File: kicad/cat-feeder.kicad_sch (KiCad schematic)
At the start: 7 parts, among them M1 Motor_Servo, M2 Motor_DC, SW1 SW_SPST, SW2 SW_Push, U1 NodeMCU1.0(ESP-12E), U2 L298N

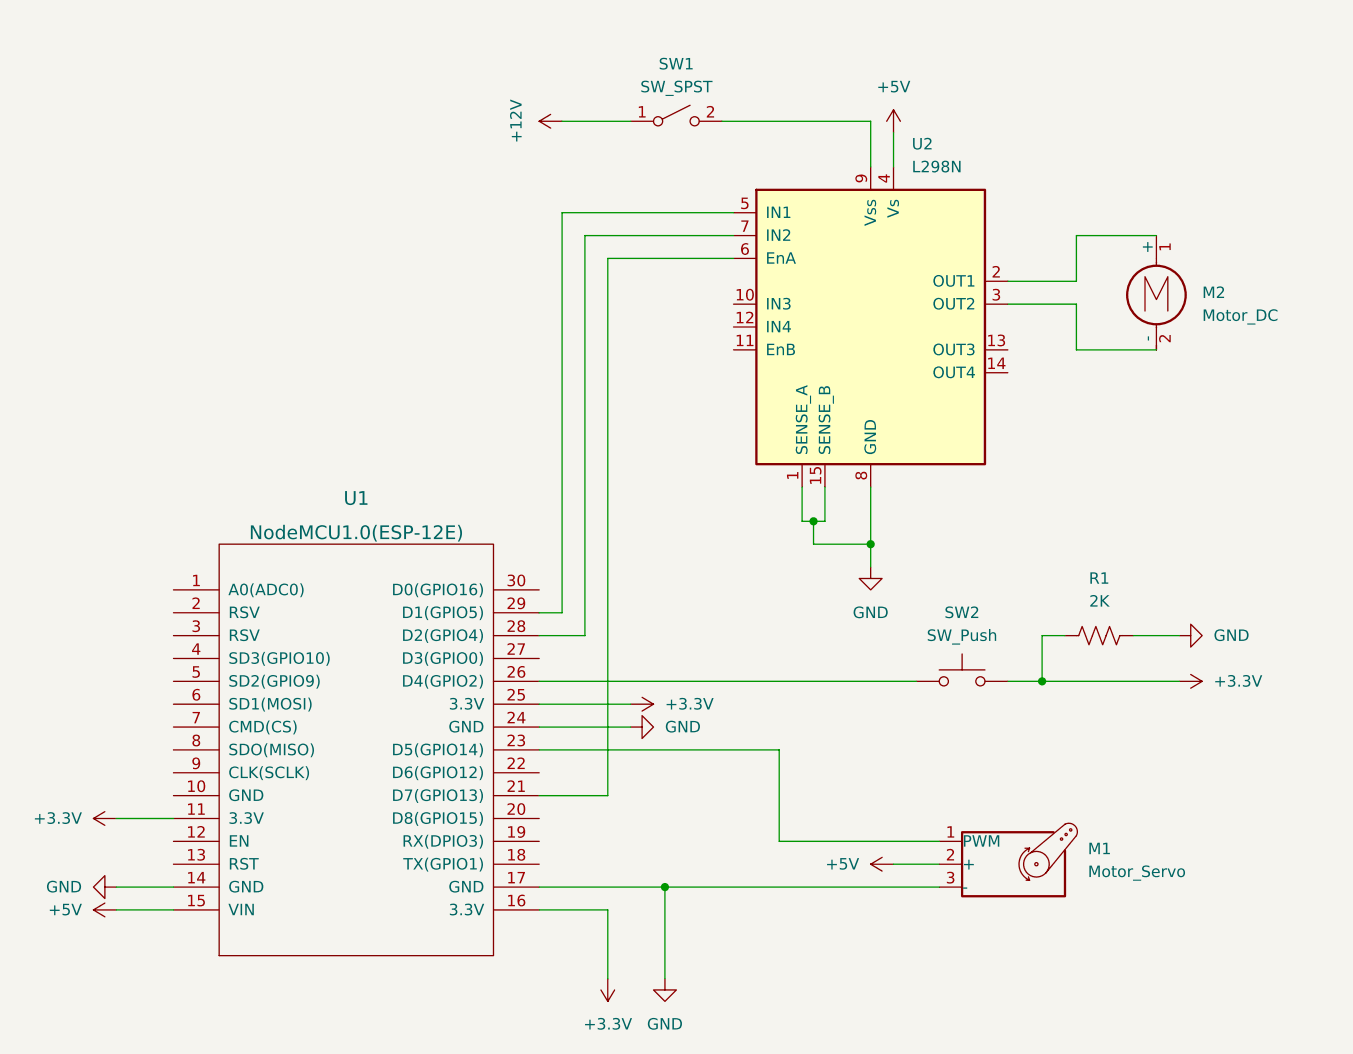
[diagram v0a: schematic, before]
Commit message: add ready and power LEDs to schematic
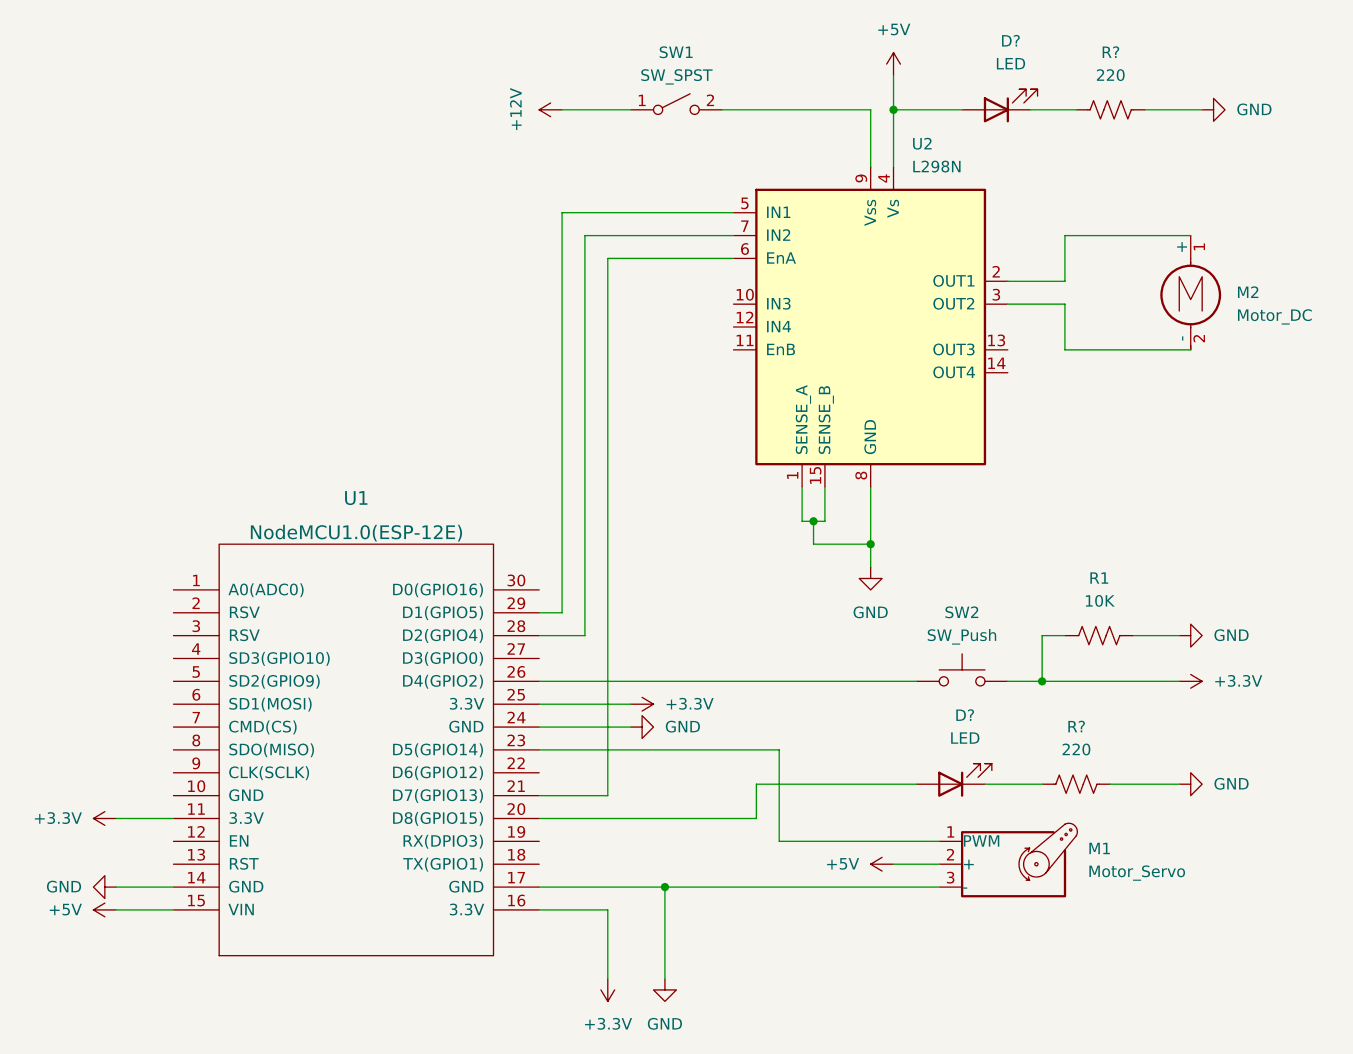
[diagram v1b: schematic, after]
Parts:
- added D? (x2): LED, symbol Device:LED
- added R? (x2): 220, symbol Device:R_US
- R1: value 2K -> 10K
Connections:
- net +5V: now also D?.2 (A)
- net GND: now also R?.2, R?.2
- net at U1.20 (D8(GPIO15)): now also D?.2 (A)
- new net: D?.1 (K), R?.1 (x2)
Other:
- moved on the sheet: M2, SW1

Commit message: change LED resistors to 470 ohm
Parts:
- R? (x2): value 220 -> 470
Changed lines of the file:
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@@
     (in_bom yes) (on_board yes) (fields_autoplaced)
     (property "Reference" "R?" (id 0) (at 166.37 107.95 90))
-    (property "Value" "220" (id 1) (at 166.37 110.49 90))
+    (property "Value" "470" (id 1) (at 166.37 110.49 90))
     (property "Footprint" "" (id 2) (at 166.624 113.284 90)
       (effects (font (size 1.27 1.27)) hide)
@@
     (in_bom yes) (on_board yes) (fields_autoplaced)
     (property "Reference" "R?" (id 0) (at 170.18 33.02 90))
-    (property "Value" "220" (id 1) (at 170.18 35.56 90))
+    (property "Value" "470" (id 1) (at 170.18 35.56 90))
     (property "Footprint" "" (id 2) (at 170.434 38.354 90)
       (effects (font (size 1.27 1.27)) hide)
@@
     )
     (path "/98ff483f-c680-47cd-8f24-3acc0f5d4892"
-      (reference "R?") (unit 1) (value "220") (footprint "")
+      (reference "R?") (unit 1) (value "470") (footprint "")
     )
     (path "/ad93abf6-cd91-4097-ad5f-237abd0904a2"
-      (reference "R?") (unit 1) (value "220") (footprint "")
+      (reference "R?") (unit 1) (value "470") (footprint "")
     )
     (path "/3f36e4ce-1226-4af1-b183-1986a281738d"

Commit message: fixes incorrect button wiring in schematic
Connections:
- net +3.3V: no longer R1.1
- net at SW2.1, U1.26 (D4(GPIO2)): now also R1.1
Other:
- moved on the sheet: R1
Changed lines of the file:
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@@
     (company "Barrett Otte")
   )
-  (junction (at 162.56 102.87) (diameter 0) (color 0 0 0 0)
+  (junction (at 139.7 87.63) (diameter 0) (color 0 0 0 0)
   )
   (junction (at 143.51 87.63) (diameter 0) (color 0 0 0 0)
   )
+  (junction (at 116.84 102.87) (diameter 0) (color 0 0 0 0)
+  )
   (junction (at 146.05 39.37) (diameter 0) (color 0 0 0 0)
   )
@@
     (stroke (width 0) (type default) (color 0 0 0 0))
   )
-  (wire (pts (xy 137.16 87.63) (xy 143.51 87.63))
+  (wire (pts (xy 137.16 87.63) (xy 139.7 87.63))
     (stroke (width 0) (type default) (color 0 0 0 0))
   )
@@
     (stroke (width 0) (type default) (color 0 0 0 0))
   )
-  (wire (pts (xy 106.68 102.87) (xy 148.59 102.87))
+  (wire (pts (xy 106.68 102.87) (xy 116.84 102.87))
     (stroke (width 0) (type default) (color 0 0 0 0))
   )
@@
     (stroke (width 0) (type default) (color 0 0 0 0))
   )
-  (wire (pts (xy 158.75 102.87) (xy 162.56 102.87))
+  (wire (pts (xy 158.75 102.87) (xy 177.8 102.87))
     (stroke (width 0) (type default) (color 0 0 0 0))
   )
@@
     (stroke (width 0) (type default) (color 0 0 0 0))
   )
+  (wire (pts (xy 139.7 97.79) (xy 139.7 87.63))
+    (stroke (width 0) (type default) (color 0 0 0 0))
+  )
   (wire (pts (xy 59.69 118.11) (xy 66.04 118.11))
     (stroke (width 0) (type default) (color 0 0 0 0))
@@
     (stroke (width 0) (type default) (color 0 0 0 0))
   )
-  (wire (pts (xy 165.1 97.79) (xy 162.56 97.79))
+  (wire (pts (xy 116.84 97.79) (xy 121.92 97.79))
     (stroke (width 0) (type default) (color 0 0 0 0))
   )
@@
     (stroke (width 0) (type default) (color 0 0 0 0))
   )
+  (wire (pts (xy 116.84 97.79) (xy 116.84 102.87))
+    (stroke (width 0) (type default) (color 0 0 0 0))
+  )
   (wire (pts (xy 114.3 115.57) (xy 106.68 115.57))
     (stroke (width 0) (type default) (color 0 0 0 0))
@@
     (stroke (width 0) (type default) (color 0 0 0 0))
   )
-  (wire (pts (xy 162.56 102.87) (xy 177.8 102.87))
-    (stroke (width 0) (type default) (color 0 0 0 0))
-  )
-  (wire (pts (xy 172.72 97.79) (xy 177.8 97.79))
+  (wire (pts (xy 129.54 97.79) (xy 139.7 97.79))
     (stroke (width 0) (type default) (color 0 0 0 0))
   )
@@
     (stroke (width 0) (type default) (color 0 0 0 0))
   )
-  (wire (pts (xy 162.56 97.79) (xy 162.56 102.87))
+  (wire (pts (xy 116.84 102.87) (xy 148.59 102.87))
+    (stroke (width 0) (type default) (color 0 0 0 0))
+  )
+  (wire (pts (xy 139.7 87.63) (xy 143.51 87.63))
     (stroke (width 0) (type default) (color 0 0 0 0))
   )
@@
     (pin "1")
   )
-  (symbol (lib_id "Device:R_US") (at 168.91 97.79 90) (unit 1)
-    (in_bom yes) (on_board yes) (fields_autoplaced)
-    (property "Reference" "R1" (id 0) (at 168.91 91.44 90))
-    (property "Value" "10K" (id 1) (at 168.91 93.98 90))
-    (property "Footprint" "" (id 2) (at 169.164 96.774 90)
-      (effects (font (size 1.27 1.27)) hide)
-    )
-    (property "Datasheet" "~" (id 3) (at 168.91 97.79 0)
-      (effects (font (size 1.27 1.27)) hide)
-    )
-    (pin "1")
-    (pin "2")
-  )
-  (symbol (lib_id "power:GND") (at 177.8 97.79 90) (unit 1)
-    (in_bom yes) (on_board yes) (fields_autoplaced)
-    (property "Reference" "#PWR012" (id 0) (at 184.15 97.79 0)
-      (effects (font (size 1.27 1.27)) hide)
-    )
-    (property "Value" "GND" (id 1) (at 181.61 97.7899 90)
-      (effects (font (size 1.27 1.27)) (justify right))
-    )
-    (property "Footprint" "" (id 2) (at 177.8 97.79 0)
-      (effects (font (size 1.27 1.27)) hide)
-    )
-    (property "Datasheet" "" (id 3) (at 177.8 97.79 0)
-      (effects (font (size 1.27 1.27)) hide)
-    )
-    (pin "1")
+  (symbol (lib_id "Device:R_US") (at 125.73 97.79 90) (unit 1)
+    (in_bom yes) (on_board yes) (fields_autoplaced)
+    (property "Reference" "R1" (id 0) (at 125.73 91.44 90))
+    (property "Value" "10K" (id 1) (at 125.73 93.98 90))
+    (property "Footprint" "" (id 2) (at 125.984 96.774 90)
+      (effects (font (size 1.27 1.27)) hide)
+    )
+    (property "Datasheet" "~" (id 3) (at 125.73 97.79 0)
+      (effects (font (size 1.27 1.27)) hide)
+    )
+    (pin "1")
+    (pin "2")
   )
   (symbol (lib_id "power:GND") (at 59.69 125.73 270) (unit 1)
@@
       (reference "#PWR011") (unit 1) (value "+5V") (footprint "")
     )
-    (path "/6f496f53-838b-4575-96a9-2ac7beb5b406"
-      (reference "#PWR012") (unit 1) (value "GND") (footprint "")
-    )
     (path "/2efd8b59-9321-47c4-9871-554b77dc38a3"
